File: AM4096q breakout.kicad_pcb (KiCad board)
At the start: 2 copper layers, 22 x 29 mm, 13 parts, among them IC1 AM4096Q

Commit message: rev 1.1
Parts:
- J1: value (none) -> Conn_01x03
- J2, J3: value (none) -> Conn_01x04
- moved R1 0.51 mm to (10.1, 2.38)
- moved R2 0.51 mm to (12.1, 2.38)
- moved R3 0.51 mm to (14.0, 2.38)
- moved IC1 0.34 mm to (11.0, 7.06)
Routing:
- net VIN: track 0.00 -> 47.6 mm
- net B: track 23.3 -> 33.3 mm, vias 1 -> 0
- net A: track 21.3 -> 28.5 mm, vias 1 -> 0
- net GND: track 9.29 -> 12.5 mm, vias 2 -> 3
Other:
- net class Default: via_dia 0.4 -> 0.5; via_drill 0.3 -> 0.4
- rule pad_to_mask_clearance: 0.2 -> 0.127
- rule via_min_drill: 0.3 -> 0.2032
- rule via_min_size: 0.35 -> 0.4572

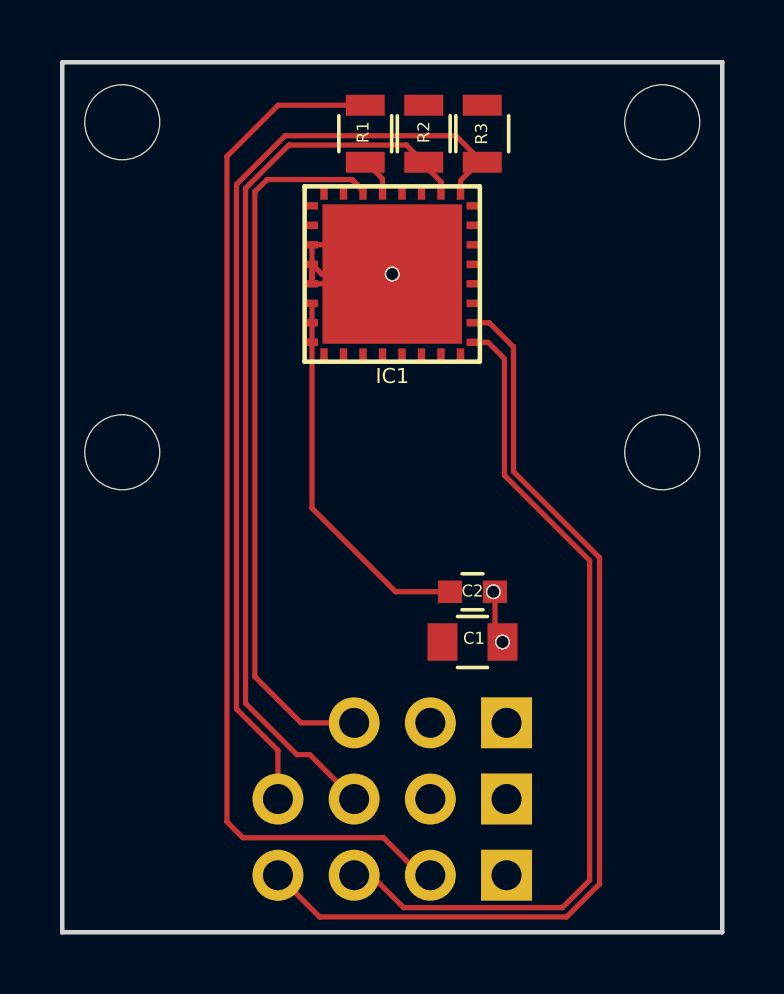
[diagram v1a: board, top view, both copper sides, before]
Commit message: Updated PCB
Updated footorint. Re-routed parts of board.
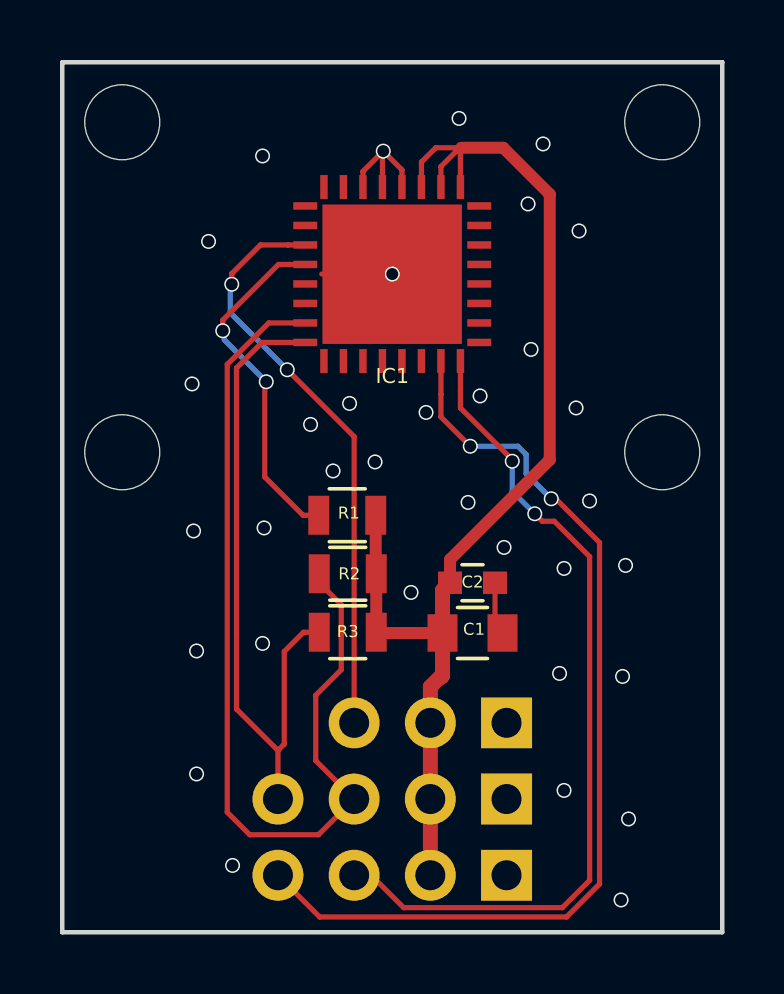
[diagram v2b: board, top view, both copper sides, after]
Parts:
- moved R3 17.2 mm to (9.52, 19.0), turned to 0 degrees
- moved R2 14.9 mm to (9.52, 17.1), turned to 0 degrees
- moved R1 12.7 mm to (9.50, 15.1), turned to 0 degrees
- moved C1 0.30 mm to (13.7, 19.0)
- moved C2 0.30 mm to (13.7, 17.4)
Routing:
- net Net-(IC1-Pad4): track 1.30 -> 11.7 mm, vias 0 -> 2
- net SCL: track 31.7 -> 22.4 mm
- net VIN: track 47.6 -> 39.3 mm
- net AOUT: track 24.1 -> 19.6 mm, vias 0 -> 2
- net GND: track 12.5 -> 10.2 mm, vias 3 -> 34
- net SDA: track 30.2 -> 31.8 mm
- net A: track 28.5 -> 28.0 mm, vias 0 -> 2
- net B: track 33.3 -> 33.2 mm, vias 0 -> 2
- added copper zone on F.Cu, net GND
- removed copper zone on F.Cu, net VIN

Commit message: Added magnet presence LED
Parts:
- added D1: LED, LEDs:LED_0805, F.Cu at (2.50, 18.9)
- added R4: 51K, Resistors_SMD:R_0805, F.Cu at (2.50, 22.8)
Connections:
- IC1 pad 1: (no net) -> Net-(IC1-Pad1)
- IC1 pad 10: (no net) -> Net-(IC1-Pad10)
- IC1 pad 11: (no net) -> Net-(IC1-Pad11)
- IC1 pad 12: (no net) -> Net-(IC1-Pad12)
- IC1 pad 13: (no net) -> Net-(IC1-Pad13)
- IC1 pad 14: (no net) -> Net-(IC1-Pad14)
- IC1 pad 17: (no net) -> Net-(IC1-Pad17)
- IC1 pad 18: (no net) -> Net-(IC1-Pad18)
- IC1 pad 19: (no net) -> Net-(IC1-Pad19)
- IC1 pad 2: (no net) -> Net-(IC1-Pad2)
- IC1 pad 20: (no net) -> Net-(IC1-Pad20)
- IC1 pad 21: (no net) -> Net-(IC1-Pad21)
- IC1 pad 22: (no net) -> Net-(IC1-Pad22)
- IC1 pad 23: (no net) -> Net-(IC1-Pad23)
- IC1 pad 24: (no net) -> Net-(IC1-Pad24)
- IC1 pad 31: (no net) -> Net-(IC1-Pad31)
- IC1 pad 32: (no net) -> Net-(D1-Pad2)
- IC1 pad 5: (no net) -> Net-(IC1-Pad5)
- IC1 pad 6: (no net) -> Net-(IC1-Pad6)
- IC1 pad 9: (no net) -> Net-(IC1-Pad9)
- J2 pad 2: VIN -> Net-(J2-Pad2)
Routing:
- net Net-(D1-Pad2): track 0.00 -> 20.1 mm
- net Net-(D1-Pad1): track 0.00 -> 1.90 mm
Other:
- rule via_min_size: 0.4572 -> 254

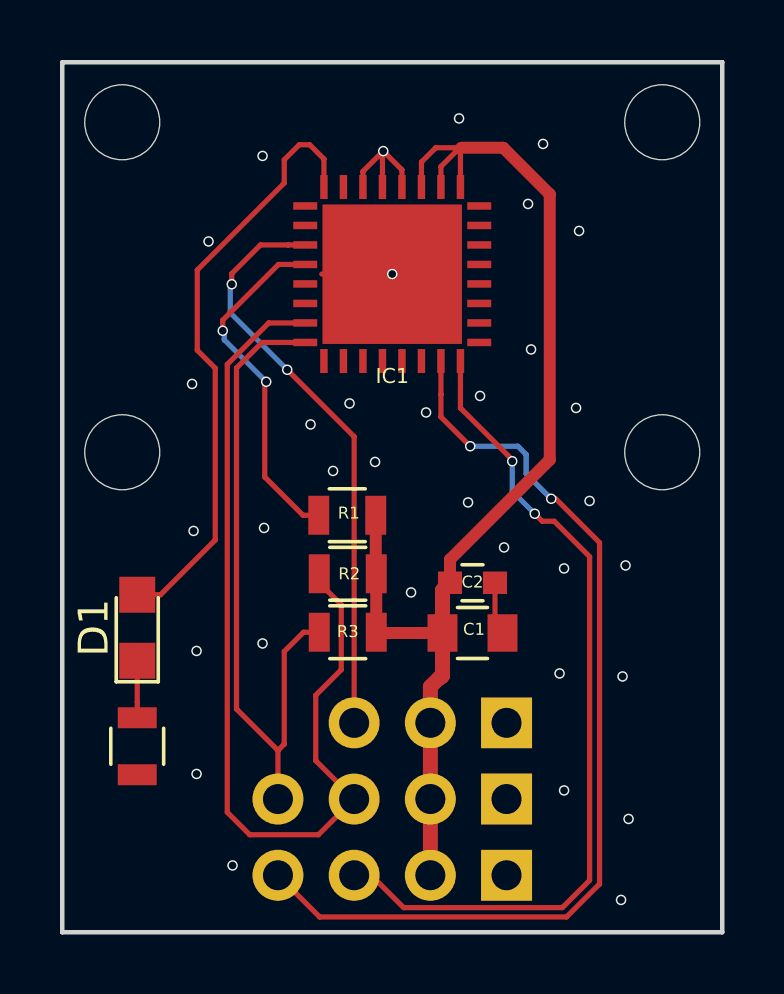
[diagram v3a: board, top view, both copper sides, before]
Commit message: Updated PCB with new required components and redid layout for single layer
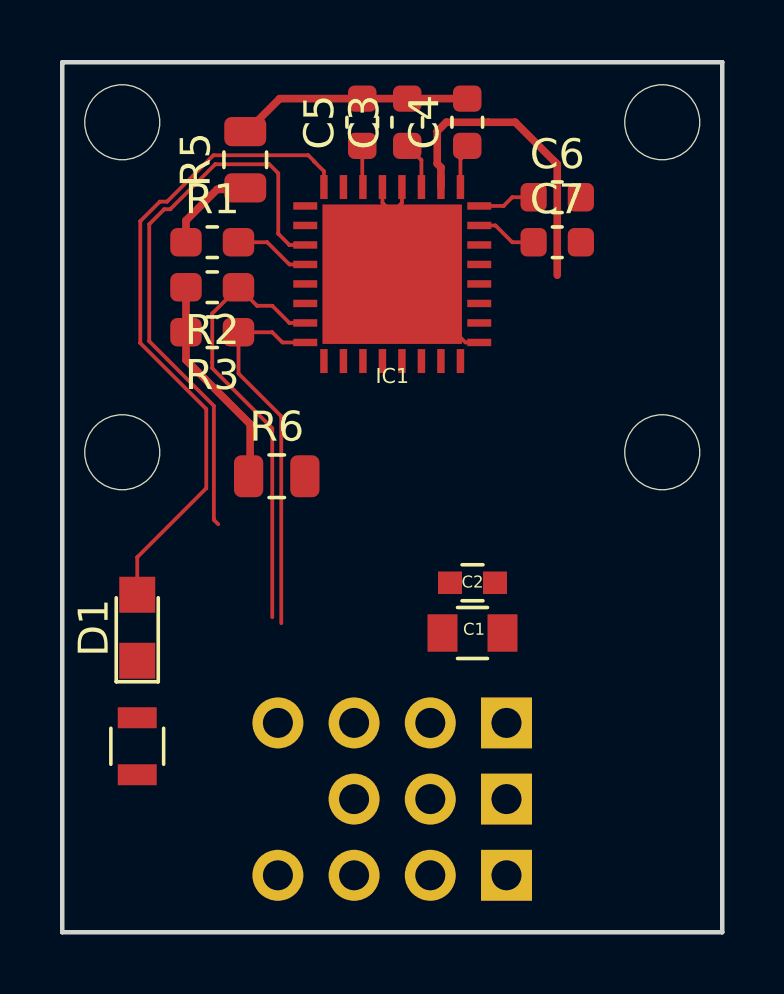
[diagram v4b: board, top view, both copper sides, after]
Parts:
- added C3: 2.2u, Capacitor_SMD:C_0603_1608Metric, F.Cu at (11.5, 2.00)
- added C4: 2.2u, Capacitor_SMD:C_0603_1608Metric, F.Cu at (13.5, 2.00)
- added C5: 100n, Capacitor_SMD:C_0603_1608Metric, F.Cu at (10.0, 2.00)
- added C6: 100n, Capacitor_SMD:C_0603_1608Metric, F.Cu at (16.5, 4.50)
- added C7: 100n, Capacitor_SMD:C_0603_1608Metric, F.Cu at (16.5, 6.00)
- added R5: 0, Resistor_SMD:R_0805_2012Metric, F.Cu at (6.10, 3.25)
- added R6: 0, Resistor_SMD:R_0805_2012Metric, F.Cu at (7.15, 13.8)
- C1: value 10UF 16V -> 10u 16v
- C2: value 100NF -> 100nf
- R1, R2, R3: footprint Resistors_SMD:R_0805 -> Resistor_SMD:R_0603_1608Metric_Pad1.05x0.95mm_HandSolder
- R4: value 51K -> 330
- moved R3 11.0 mm to (5.00, 9.00), turned to 180 degrees
- moved R2 10.6 mm to (5.00, 7.50), turned to 180 degrees
- moved R1 10.2 mm to (5.00, 6.00)
- moved J1 2.54 mm to (14.8, 24.6)
- moved J2 2.54 mm to (14.8, 22.0)
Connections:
- C1 pad 1: VIN -> VCC
- C2 pad 1: VIN -> VCC
- IC1 pad 17: Net-(IC1-Pad17) -> GND
- IC1 pad 25: VIN -> Net-(C4-Pad1)
- IC1 pad 26: VIN -> VCC
- IC1 pad 27: VIN -> Net-(C3-Pad1)
- IC1 pad 30: GND -> Net-(C5-Pad1)
- J1 pad 2: VIN -> VCC
- J2 pad 2: Net-(J2-Pad2) -> VCC
- J3 pad 2: VIN -> VCC
- R1 pad 1: Net-(IC1-Pad4) -> GND
- R1 pad 2: VIN -> Net-(IC1-Pad4)
- R2 pad 2: VIN -> VCC
- R3 pad 2: VIN -> VCC
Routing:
- net VIN: track 39.3 -> 0.00 mm
- net B: track 33.2 -> 0.00 mm, vias 2 -> 0
- net A: track 28.0 -> 0.00 mm, vias 2 -> 0
- net VCC: track 0.00 -> 17.5 mm
- net SDA: track 31.8 -> 14.9 mm
- net SCL: track 22.4 -> 12.7 mm
- net Net-(IC1-Pad4): track 11.7 -> 2.53 mm, vias 2 -> 0
- net GND: track 10.2 -> 18.9 mm, vias 34 -> 0
- net Net-(C7-Pad1): track 0.00 -> 2.04 mm
- net Net-(D1-Pad2): track 20.1 -> 22.1 mm
- net Net-(C6-Pad1): track 0.00 -> 1.93 mm
- net Net-(D1-Pad1): track 1.90 -> 0.00 mm
- net Net-(C3-Pad1): track 0.00 -> 1.88 mm
- net Net-(C4-Pad1): track 0.00 -> 1.47 mm
- net Net-(C5-Pad1): track 0.00 -> 1.38 mm
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- removed copper zone on F.Cu, net GND
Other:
- net class Default: trace_width 0.175 -> 0.127
- rule via_min_size: 254 -> 0.381
